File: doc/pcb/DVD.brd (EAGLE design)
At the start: 48.1 x 42.3 mm, 48 parts, among them IC1 7805, IC2 74HC14N

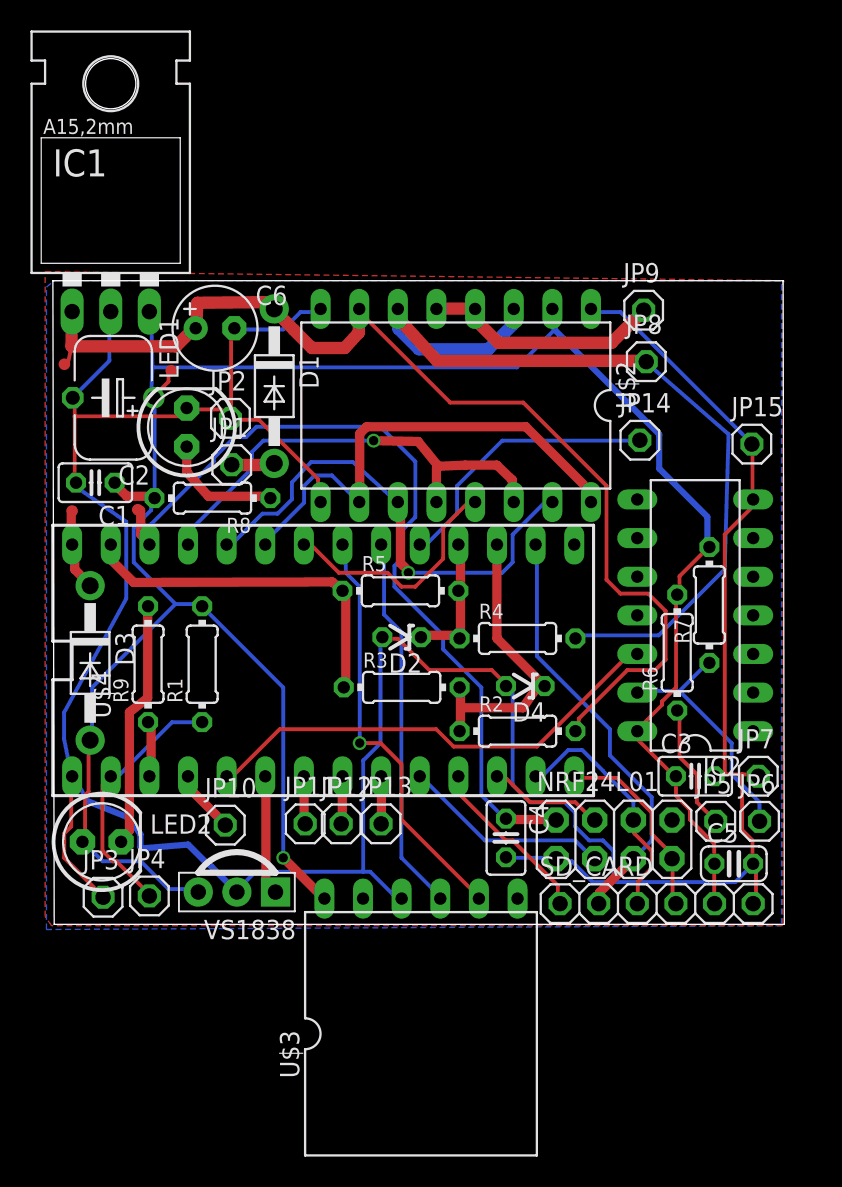
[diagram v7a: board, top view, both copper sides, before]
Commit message: PCB: new pads, ripup, partial route
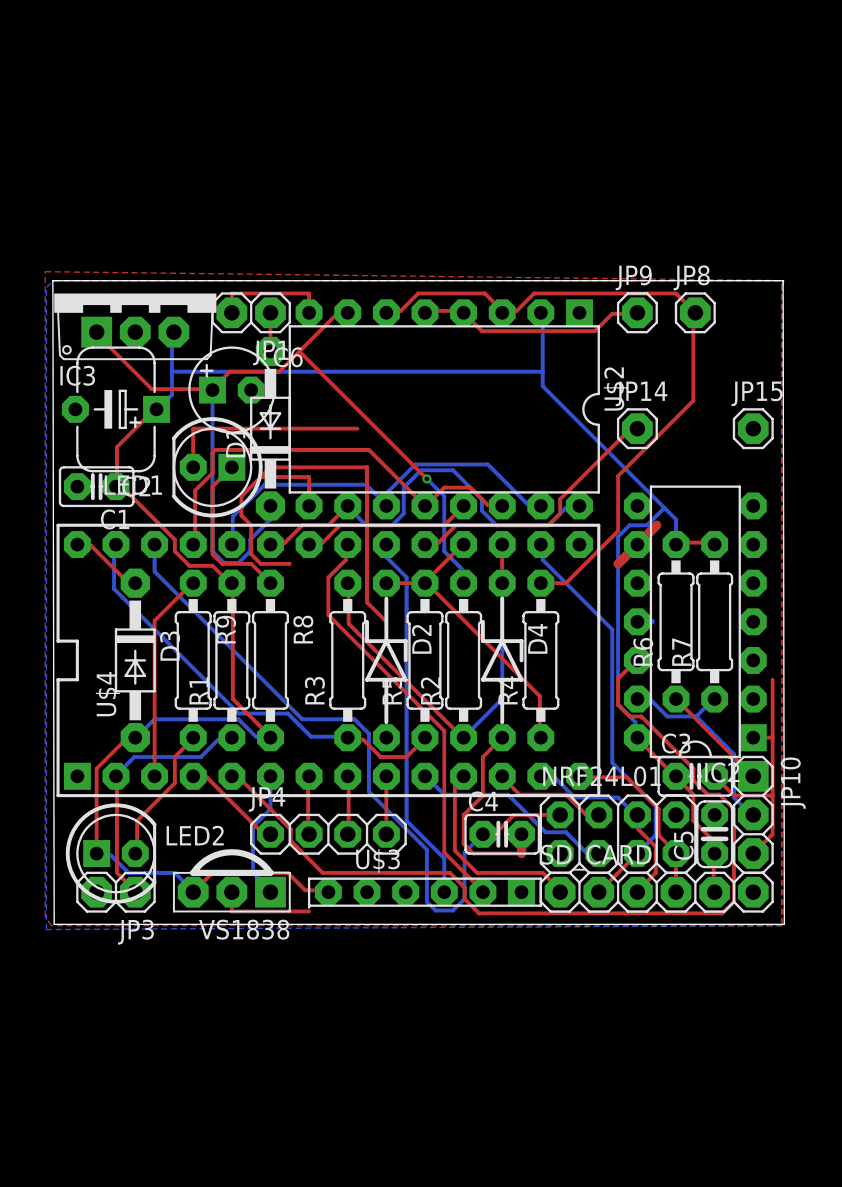
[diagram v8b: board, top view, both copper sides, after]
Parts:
- removed IC1: 7805, v-reg:78XXL
- removed JP11: P5, pinhead:1X01
- removed JP12: P6, pinhead:1X01
- removed JP13: P7, pinhead:1X01
- removed JP2: Pick-up -, pinhead:1X01
- removed JP5: Car Speed Sensor Red, pinhead:1X01
- removed JP6: Car Speed Sensor Brown, pinhead:1X01
- removed JP7: Car Speed Sensor Yellow, pinhead:1X01
- removed TP1: TEST-POINT1, SparkFun-Passives:PAD.03X.03
- removed TP2: TEST-POINT2, SparkFun-Passives:PAD.03X.03
- removed TP3: TEST-POINT3, SparkFun-Passives:PAD.03X.03
- removed TP4: TEST-POINT4, SparkFun-Passives:PAD.03X.03
- added IC3: 7805, linear:TO220V
- D2, D4: device diode:ZDIO-2.5 -> diode:ZDIO-7.5
- JP1: value Pick-up + -> Pick-up; device pinhead:1X01 -> pinhead:1X02
- JP10: value P2 -> Car Speed Sensor; device pinhead:1X01 -> pinhead:1X03
- JP3: value Chassis Switch 1 -> Chassis Switch; device pinhead:1X01 -> pinhead:1X02
- JP4: value Chassis Switch 2 -> (none); device pinhead:1X01 -> pinhead:1X04
- R1, R2, R3, R4, R5, R6, R7, R8, R9: device resistor:0204/7 -> resistor:0207/10
- moved JP10 34.7 mm to (50.8, 7.62), turned to 270 degrees
- moved JP4 12.5 mm to (22.9, 6.35)
- moved R8 11.3 mm to (19.1, 17.8), turned to 270 degrees
- moved JP1 10.1 mm to (17.8, 40.6), turned to 180 degrees
- moved U$3 9.32 mm to (29.2, 2.54)
- moved R2 5.85 mm to (31.8, 17.8), turned to 90 degrees
- moved R5 4.85 mm to (29.2, 17.8), turned to 90 degrees
- moved JP8 4.56 mm to (47.0, 40.6)
- moved C6 4.22 mm to (16.5, 35.6)
- moved R3 3.96 mm to (24.1, 17.8), turned to 90 degrees
- moved LED1 3.13 mm to (15.2, 30.5), turned to 180 degrees
- moved R9 2.98 mm to (14.0, 17.8), turned to 270 degrees
- moved D3 2.97 mm to (10.2, 17.8)
- moved D1 2.81 mm to (19.1, 33.0), turned to 90 degrees
- moved C5 2.31 mm to (48.3, 6.35), turned to 90 degrees
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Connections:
- net +3V3: no longer TP2.P$1
- net +5V: now also IC3.3; no longer IC1.OUT, TP1.P$1
- net GND: now also JP1.2, JP10.3, JP3.2; no longer IC1.GND, JP2.1, JP3.1, JP7.1
- net N$1: no longer TP4.P$1
- net N$18: now also JP3.1; no longer JP4.1
- net N$2: now also JP10.1; no longer JP5.1
- net N$20: now also JP4.1; no longer JP10.1
- net N$21: now also JP4.3; no longer JP12.1
- net N$22: now also JP4.4; no longer JP13.1
- net N$26: now also JP10.2; no longer JP6.1
- net N$3: now also JP4.2; no longer JP11.1
- net V+: now also IC3.1; no longer IC1.IN, TP3.P$1
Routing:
- net GND: track 212.8 -> 93.6 mm
- net SPEED_SENSOR: track 31.3 -> 58.4 mm
- net V+: track 71.5 -> 57.3 mm, vias 0 -> 1
- net JP8: track 57.1 -> 45.5 mm
- net N$11: track 9.15 -> 19.6 mm
- net N$19: track 3.80 -> 13.8 mm
- net +3V3: track 55.7 -> 46.3 mm
- net N$8: track 0.00 -> 8.89 mm
- net N$10: track 19.8 -> 27.1 mm
- net +5V: track 153.4 -> 146.2 mm, vias 1 -> 0
- net N$4: track 16.3 -> 9.21 mm
- net IN2: track 32.6 -> 26.6 mm, vias 1 -> 0
- net AGND: track 23.5 -> 28.6 mm
- net PWM: track 31.8 -> 27.0 mm
- net STBY: track 15.9 -> 11.2 mm
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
